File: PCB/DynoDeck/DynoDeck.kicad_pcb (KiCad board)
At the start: 4 copper layers, 105 x 107.3 mm, 76 parts, among them J1 USB_C_Receptacle_USB2.0_16P, J2 PGRM, J3 CardKBConn, J4 E-paper, J5 HC-IPEX0125-01 (u.FL), J6 BWSMA-KWE-Z001 (SMA), J7 CardKBRef, SW1 QON, SW2 POWER, SW3 RESET, SW4 IO1, U1 BQ25895RTW, U2 USBLC6-2SC6, U3 SX1262IMLTRT, U4 TUSB320, U5 MD7218E33PC1, U6 E73-2G4M08S1C, U7 PE42422MLAA-Z, U8 PE42422MLAA-Z, Y1 OW7EL89CENUXK7YLC-32M, Y3 3N00032G33YC

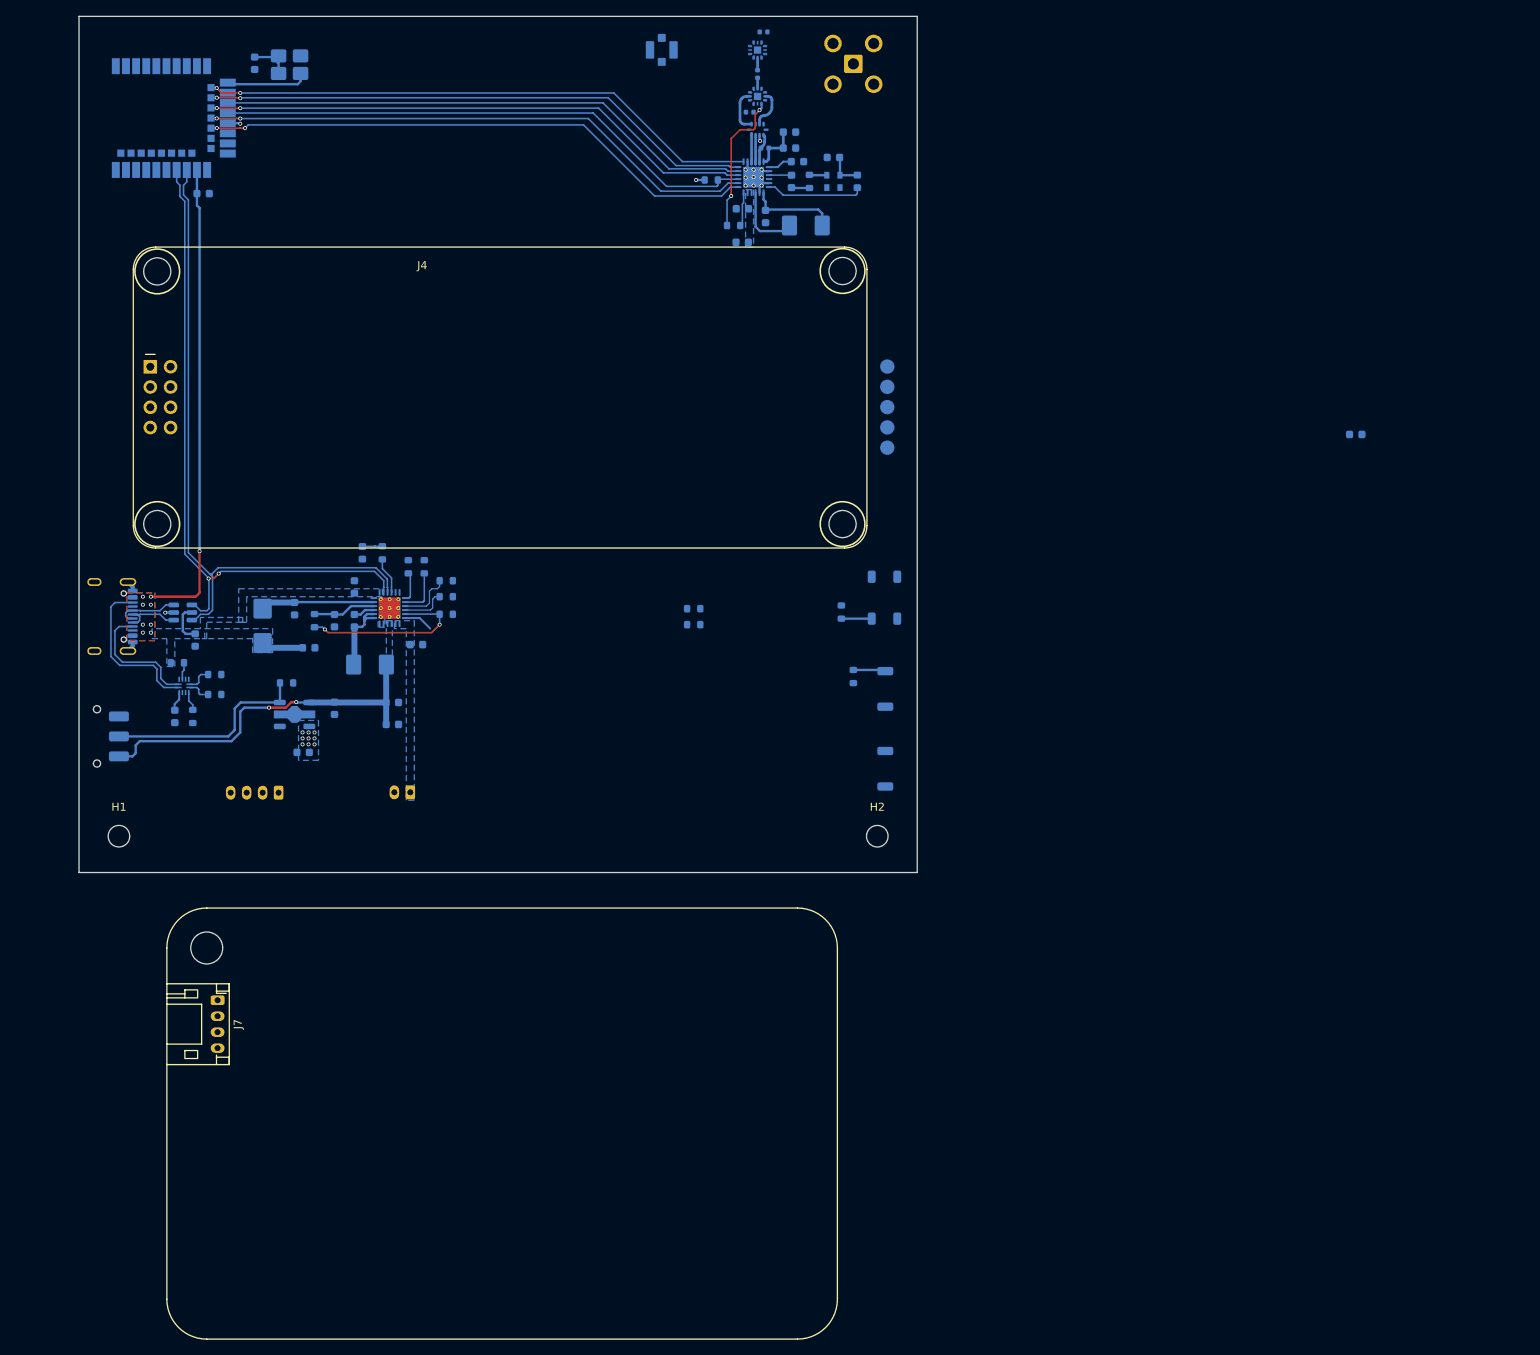
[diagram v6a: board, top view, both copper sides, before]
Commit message: Bit of routing of Screen
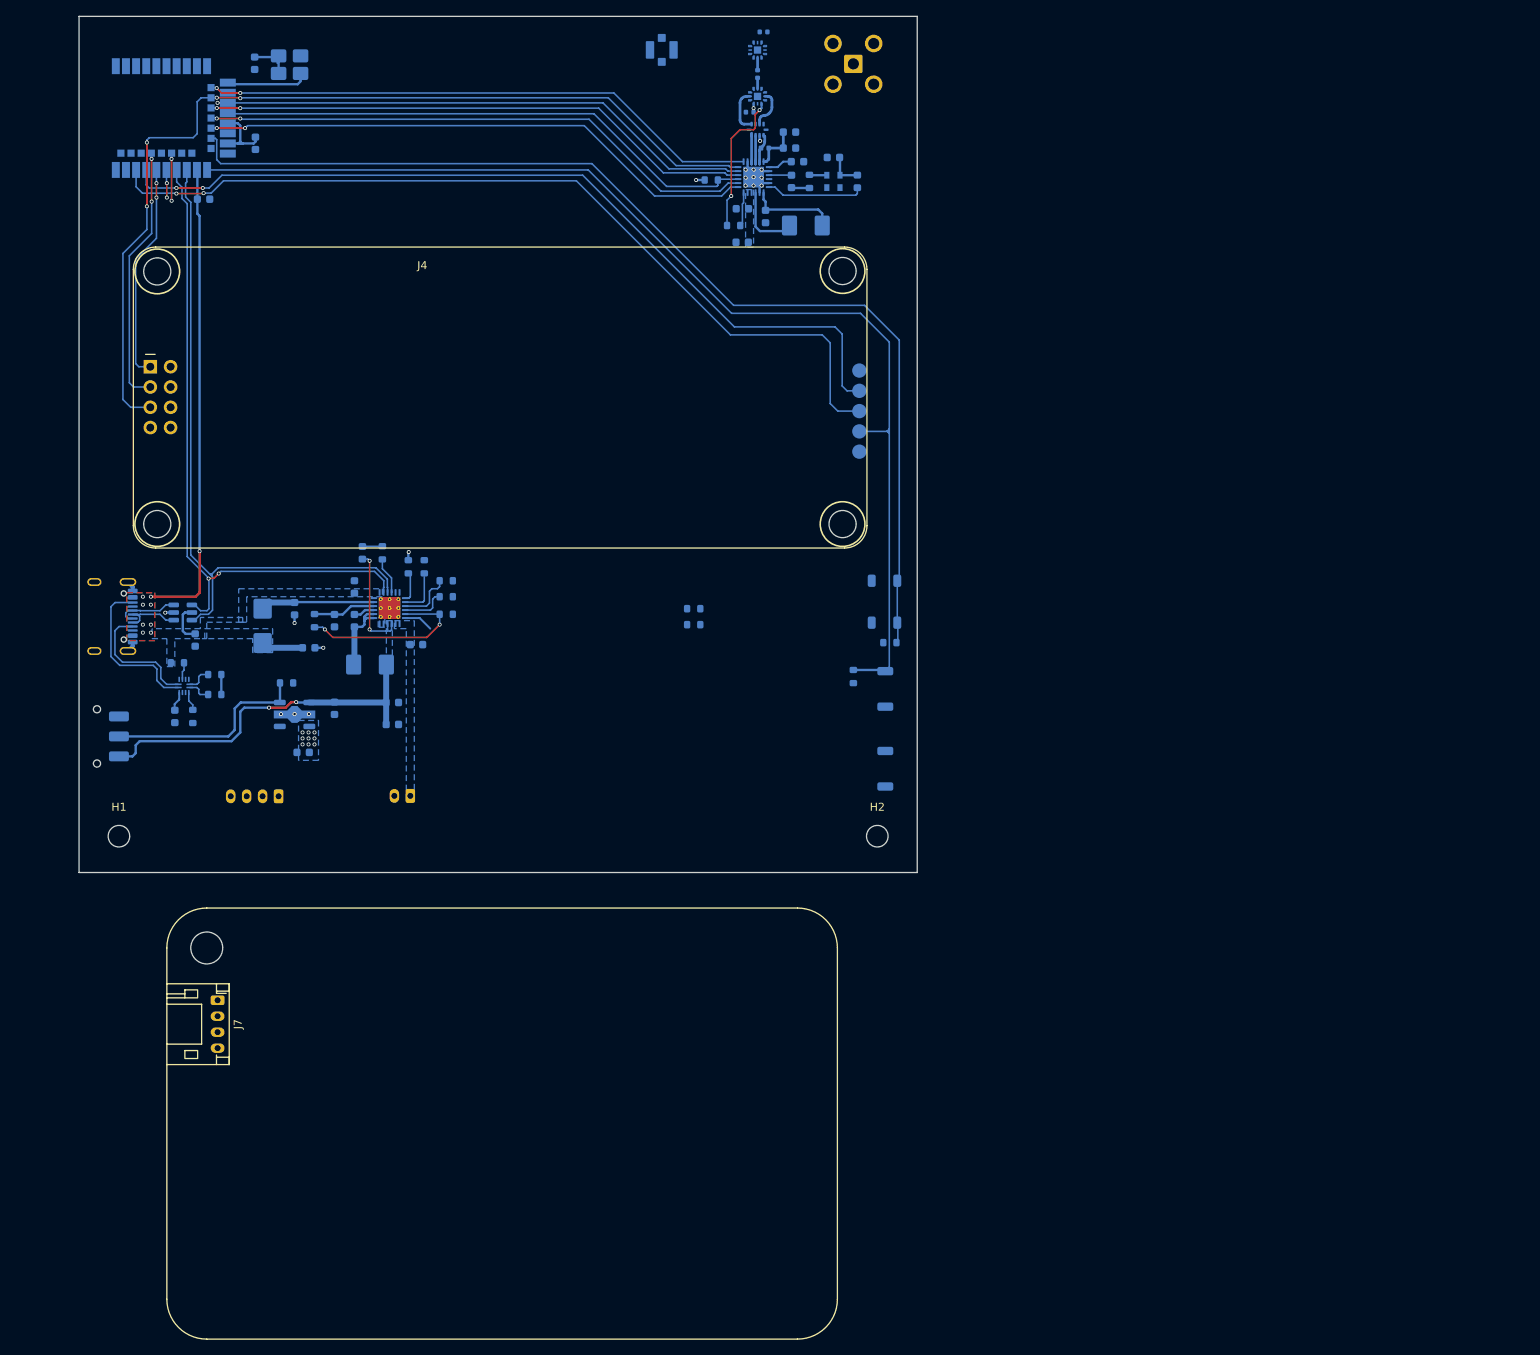
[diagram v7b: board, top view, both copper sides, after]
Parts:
- moved C21 142.6 mm to (52.1, 44.2), turned to -90 degrees
- moved R18 7.18 mm to (131.6, 106.8), turned to 0 degrees
- moved J2 3.54 mm to (127.8, 72.7)
- moved C20 0.70 mm to (45.6, 51.2)
- moved SW4 0.50 mm to (130.9, 101.6), turned to 90 degrees
- moved BT1 0.45 mm to (71.5, 126.0)
- moved J3 0.45 mm to (55.0, 126.0)
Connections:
- J2 pad 2: /SWDCLK -> /SWDIO
- J2 pad 3: /SWDIO -> /SWDCLK
- U6 pad 22: unconnected-(U6B-P0.07-Pad22) -> /USER1
- U6 pad 28: /RES -> unconnected-(U6B-P0.15-Pad28)
- U6 pad 32: unconnected-(U6B-P0.20-Pad32) -> /ENSS
- U6 pad 33: unconnected-(U6B-P0.13-Pad33) -> /RES
- U6 pad 34: /ENSS -> unconnected-(U6B-P0.22-Pad34)
- U6 pad 36: /USER1 -> /DC
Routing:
- net /nRESET: track 4.06 -> 144.4 mm
- net /USER1: track 3.80 -> 136.4 mm
- net /SWDCLK: track 0.00 -> 110.1 mm, vias 0 -> 2
- net /SWDIO: track 0.00 -> 107.0 mm, vias 0 -> 2
- net /SCK: track 69.7 -> 119.8 mm, vias 2 -> 4
- net /DC: track 0.00 -> 32.8 mm, vias 0 -> 2
- net /EBUSY: track 0.00 -> 27.3 mm, vias 0 -> 2
- net /SYS: track 45.9 -> 60.2 mm, vias 2 -> 4
- net +3V3: track 13.4 -> 25.2 mm, vias 11 -> 12
- net /ENSS: track 0.00 -> 5.97 mm, vias 0 -> 2
- net /RES: track 0.00 -> 3.48 mm, vias 0 -> 2
- net GND: track 11.3 -> 13.5 mm, vias 11 -> 16
- net /MOSI: track 67.5 -> 68.8 mm, vias 0 -> 1

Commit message: TUSB320 wiring to nRF
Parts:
- moved R2 41.1 mm to (68.0, 91.5), turned to 0 degrees
- moved R4 36.7 mm to (72.0, 91.5)
- moved C20 1.27 mm to (46.9, 51.2)
- moved J6 0.96 mm to (126.9, 33.3)
- moved J5 0.50 mm to (103.0, 32.0)
- moved R15 0.28 mm to (42.3, 109.0)
- turned SW1 to 90 degrees
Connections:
- U6 pad 1: /OUT1 -> unconnected-(U6C-P1.11-Pad1)
- U6 pad 2: /OUT2 -> unconnected-(U6C-P1.10-Pad2)
- U6 pad 3: /ID -> unconnected-(U6B-P0.03/AIN1-Pad3)
- U6 pad 32: /ENSS -> unconnected-(U6B-P0.20-Pad32)
- U6 pad 33: /RES -> /ENSS
- U6 pad 34: unconnected-(U6B-P0.22-Pad34) -> /RES
- U6 pad 41: unconnected-(U6B-P0.09/NFC1-Pad41) -> /OUT1
- U6 pad 42: unconnected-(U6C-P1.06-Pad42) -> /OUT2
- U6 pad 43: unconnected-(U6B-P0.10/NFC2-Pad43) -> /ID
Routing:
- net /OUT2: track 2.96 -> 82.9 mm, vias 0 -> 4
- net /ANT_CTRL: track 0.00 -> 79.6 mm, vias 0 -> 2
- net /ID: track 2.38 -> 81.5 mm
- net Net-(U1-~{QON}): track 3.69 -> 79.1 mm
- net /OUT1: track 3.25 -> 78.3 mm, vias 0 -> 2
- net /MOSI: track 68.8 -> 113.7 mm, vias 1 -> 2
- net /RES: track 3.48 -> 27.8 mm
- net /ENSS: track 5.97 -> 29.0 mm
- net /~{CE}: track 6.93 -> 28.4 mm, vias 0 -> 4
- net unconnected-(U6B-P0.17-Pad30): track 0.00 -> 11.7 mm, vias 0 -> 2
- net /ANT1: track 0.00 -> 11.4 mm
- net /ANT2: track 0.00 -> 11.3 mm
- net unconnected-(U6B-P0.15-Pad28): track 0.00 -> 11.1 mm, vias 0 -> 2
- net GND: track 13.5 -> 18.2 mm, vias 16 -> 19
- net +3V3: track 25.2 -> 29.1 mm, vias 12 -> 14
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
